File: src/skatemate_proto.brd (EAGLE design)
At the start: 160 x 100 mm, 73 parts, among them IC1 REG1117, Q1 IRF740, Q2 IRF740, Q3 IRF740, Q4 IRF740, Q5 IRF740, Q6 IRF740, U1 DRV8301DCAR, U2 STM32F303RCT6

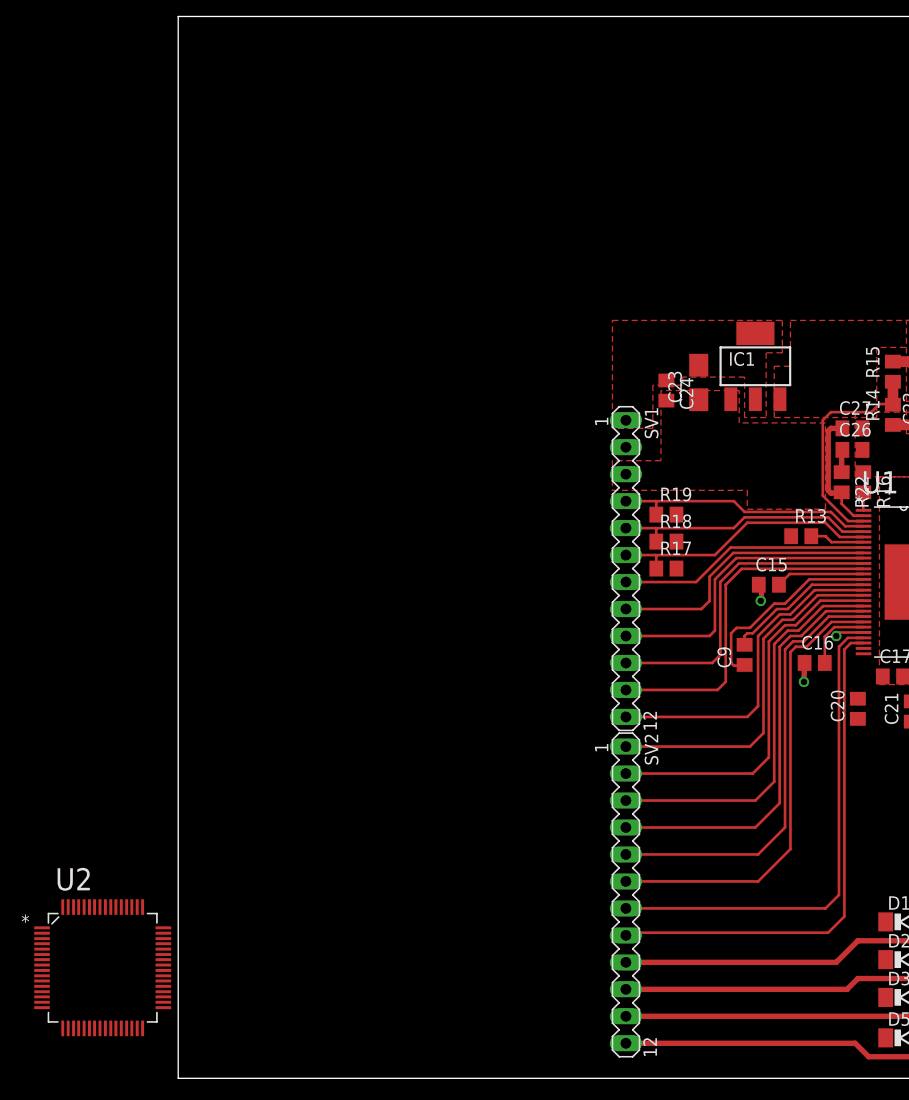
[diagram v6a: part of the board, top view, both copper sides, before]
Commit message: more digital layout
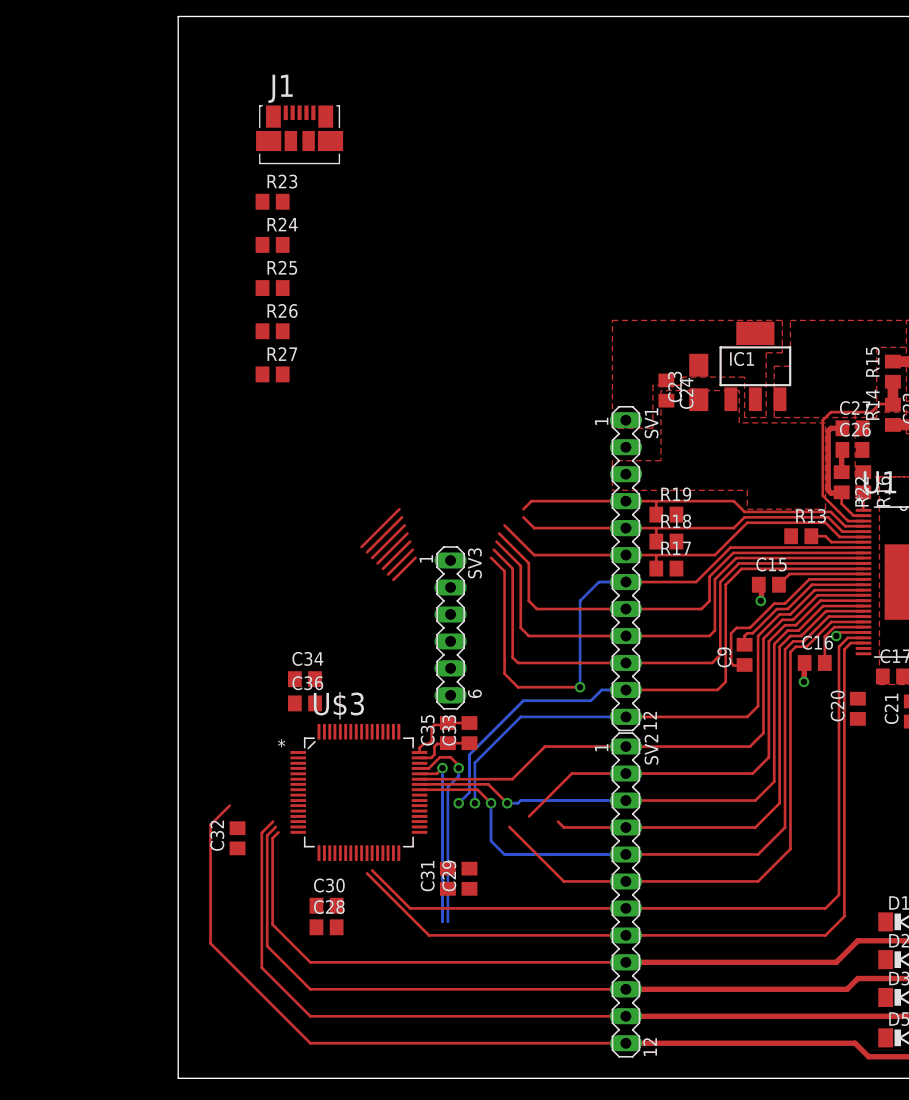
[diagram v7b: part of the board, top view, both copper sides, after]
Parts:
- removed U2: STM32F303RCT6, skatemate:QFP50P1200X1200X160-64N
- added C28, C29, C33, C34: 2u2, skatemate:C0805
- added C30, C31, C32, C35, C36: 100n, skatemate:C0805
- added J1: (no value), skatemate:MOLEX_47346-0001
- added R23: 100k, skatemate:R0805
- added R24, R25: 22, skatemate:R0805
- added R26: 1k5, skatemate:R0805
- added R27: 0 *, skatemate:R0805
- added SV3: (no value), skatemate:MA06-1
- added U$3: STM32F303XD/XE, skatemate:QFP50P1200X1200X160-64N
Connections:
- removed net VBAT: U2.1
- removed net VDDA: U2.13
- removed net VDD_1: U2.64
- removed net VDD_2: U2.32
- removed net VDD_3: U2.48
- removed net VDD_4: U2.19
- removed net VSSA/VREF-: U2.12
- new net N$22: J1.4, R23.1
- new net N$23: J1.3, R24.1, R26.1
- new net N$24: J1.2, R25.1
- new net N$25: J1.1, R27.1
- new net NRST: SV3.5, U$3.7
- new net SWCLK: SV3.2, U$3.49
- new net SWDIO: SV3.4, U$3.46
- new net USB_D+: R24.2, U$3.45
- new net USB_D-: R25.2, U$3.44
- net ASENSE: now also U$3.16
- net BSENSE: now also U$3.15
- net CSENSE: now also U$3.14
- net DRV_DCCAL: now also U$3.38
- net DRV_EN_GATE: now also U$3.37
- net DRV_NCS: now also U$3.50
- net DRV_NFAULT: now also U$3.54
- net DRV_NOCTW: now also U$3.55
- net DRV_PWRGD: now also U$3.56
- net DRV_SCK: now also U$3.51
- net DRV_SDI: now also U$3.53
- net DRV_SDO: now also U$3.52
- net DRV_SOA: now also U$3.27
- net DRV_SOB: now also U$3.26
- net GND: now also C28.1, C29.1, C30.1, C31.1, C32.1, C33.1, C34.1, C35.1, C36.1, J1.5, R23.2, SV3.3, U$3.12, U$3.18, U$3.31, U$3.47, U$3.63
- net INH_A: now also U$3.43
- net INH_B: now also U$3.42
- net INH_C: now also U$3.41
- net INL_A: now also U$3.36
- net INL_B: now also U$3.35
- net INL_C: now also U$3.34
- net SSENSE: now also U$3.11
- net VCC: now also C28.2, C29.2, C30.2, C31.2, C32.2, C33.2, C34.2, C35.2, C36.2, R26.2, R27.2, SV3.1, U$3.1, U$3.13, U$3.19, U$3.32, U$3.48, U$3.64
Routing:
- net SSENSE: track 51.0 -> 107.8 mm
- net CSENSE: track 71.9 -> 122.3 mm
- net BSENSE: track 88.1 -> 135.1 mm
- net ASENSE: track 109.6 -> 153.2 mm
- net DRV_NCS: track 23.7 -> 58.9 mm, vias 0 -> 1
- net DRV_SOB: track 48.5 -> 75.3 mm
- net DRV_SOA: track 46.6 -> 72.0 mm
- net DRV_SCK: track 30.3 -> 55.4 mm
- net INH_C: track 41.5 -> 65.5 mm, vias 0 -> 1
- net DRV_SDO: track 28.2 -> 51.2 mm
- net DRV_DCCAL: track 32.5 -> 54.7 mm, vias 0 -> 1
- net DRV_SDI: track 25.9 -> 46.9 mm
- net INH_B: track 37.6 -> 58.3 mm, vias 0 -> 1
- net INH_A: track 33.5 -> 54.2 mm
- net DRV_EN_GATE: track 31.2 -> 51.0 mm, vias 0 -> 1
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
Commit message: lqfp64 and layout
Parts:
- U$3: value STM32F303XD/XE -> STM32F303XD/XELQFP64; device skatemate:QFP50P1200X1200X160-64N -> skatemate:LQFP64
- moved C20 7.84 mm to (71.1, 38.1), turned to 0 degrees
- moved C21 2.54 mm to (71.1, 36.1), turned to 0 degrees
- moved C28 2.54 mm to (12.4, 16.3)
- moved C30 2.54 mm to (12.4, 18.3)
- moved C17 1.80 mm to (65.5, 38.1), turned to 180 degrees
- moved C32 0.92 mm to (6.10, 23.4), turned to 270 degrees
- moved C29 0.76 mm to (27.4, 19.6)
- moved C31 0.76 mm to (25.4, 19.6)
- moved C34 0.57 mm to (11.4, 37.3), turned to 180 degrees
- moved C36 0.51 mm to (11.4, 35.3), turned to 180 degrees
- moved U$3 0.25 mm to (16.8, 26.9)
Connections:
- net +5V: now also SV1.3; no longer SV1.2
- net GND: now also SV1.2; no longer SV1.3
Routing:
- net VCC: track 9.91 -> 170.4 mm, vias 1 -> 9
- net GND: track 111.7 -> 150.0 mm, vias 24 -> 27
- net SUPPLY: track 119.4 -> 155.4 mm, vias 1 -> 3
- net DRV_PWRGD: track 39.6 -> 68.7 mm
- net DRV_NOCTW: track 39.4 -> 67.9 mm
- net DRV_NFAULT: track 42.4 -> 68.5 mm
- net DRV_SDI: track 46.9 -> 71.9 mm
- net DRV_SDO: track 51.2 -> 75.4 mm
- net DRV_SCK: track 55.4 -> 78.8 mm
- net NRST: track 0.00 -> 22.7 mm
- net DRV_NCS: track 58.9 -> 81.5 mm
- net +5V: track 1.86 -> 22.2 mm
- net SWDIO: track 0.00 -> 20.1 mm
- net SWCLK: track 0.00 -> 18.1 mm
- net INL_B: track 46.1 -> 60.0 mm
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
